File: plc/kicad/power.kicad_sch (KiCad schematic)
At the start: 29 parts, among them CN14 DB128V-5.08-2P-GN-S, U13 TPS54560DDAR, U15 TPS26630RGER

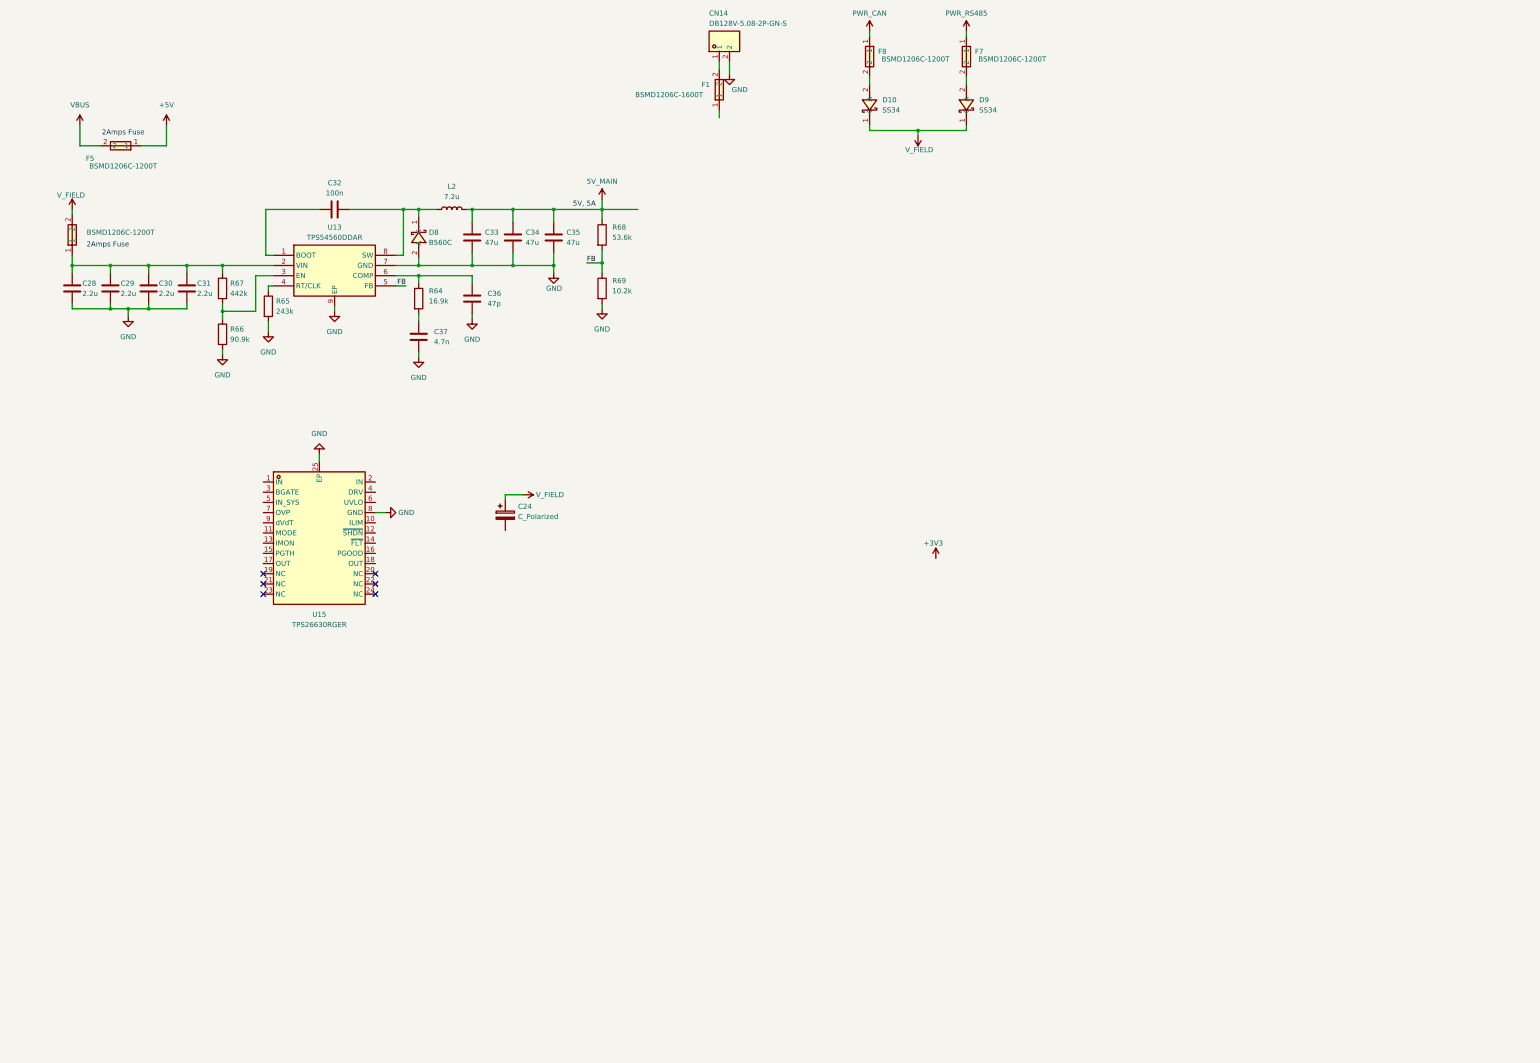
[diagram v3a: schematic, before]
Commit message: Added the power protection IC
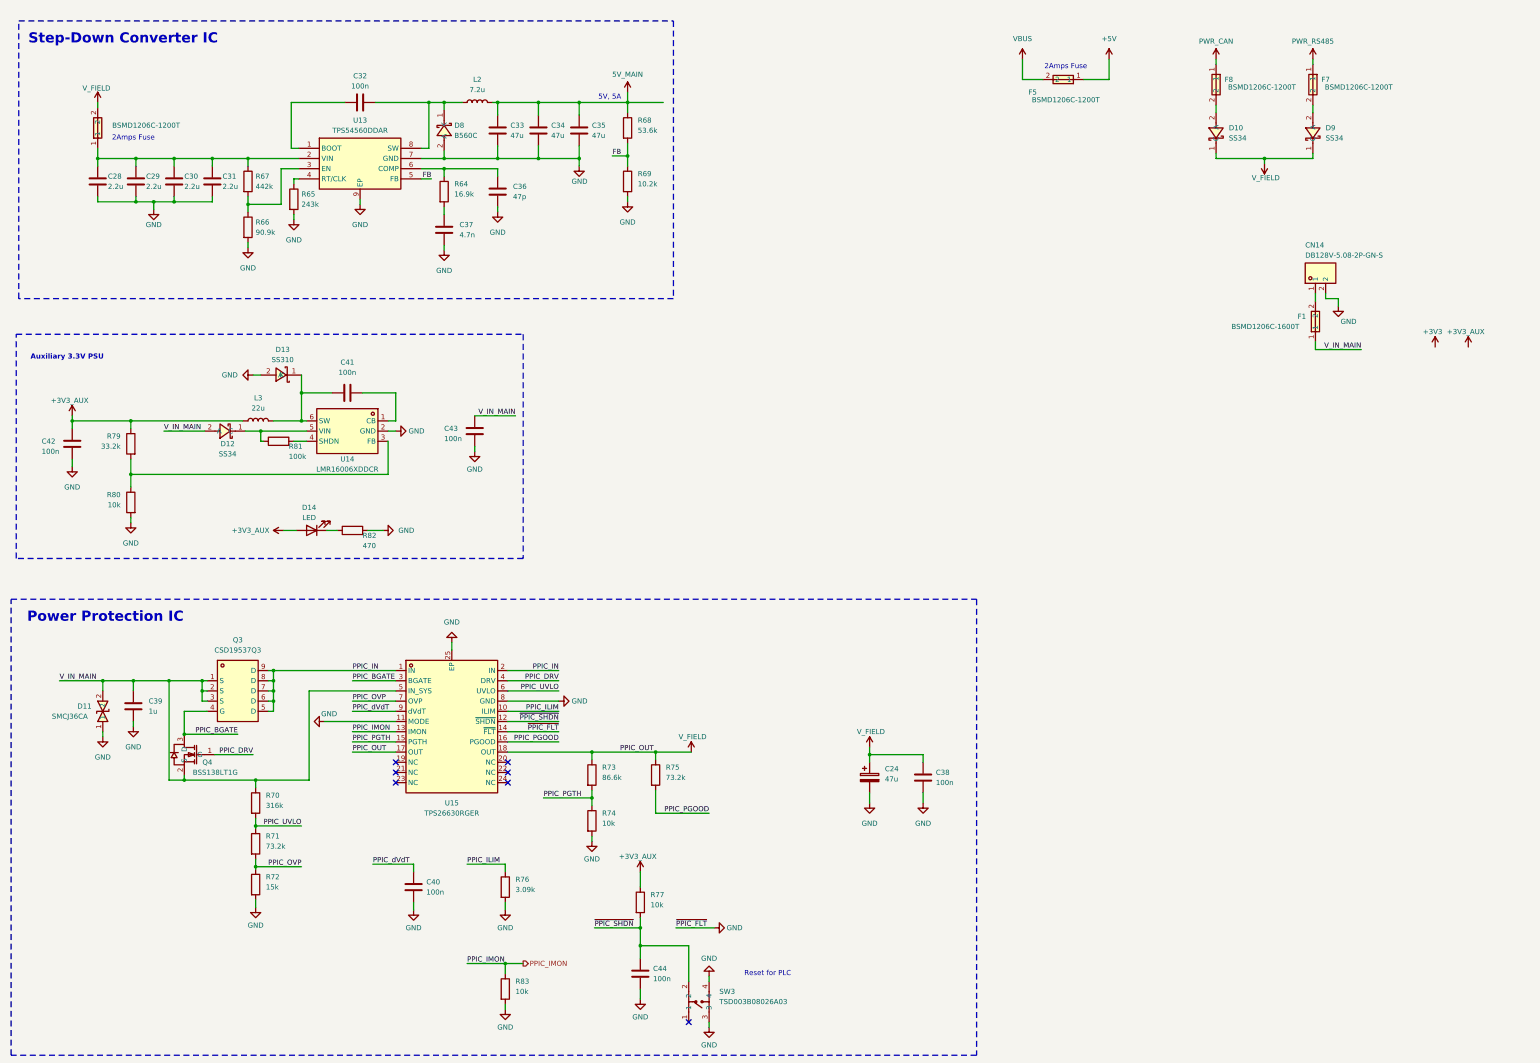
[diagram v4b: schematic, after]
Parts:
- added C38, C40, C41, C42, C43, C44: 100n, Capacitor_SMD:C_0805_2012Metric, symbol Device:C
- added C39: 1u, Capacitor_SMD:C_0805_2012Metric, symbol Device:C
- added D11: SMCJ36CA, LibrePLC32:SMC_L6.9-W5.9-LS7.9-BI, symbol LibrePLC32:SMCJ36CA-C151283
- added D12: SS34, LibrePLC32:SMA_L4.3-W2.7-LS5.1-RD, symbol LibrePLC32:SS34_C908680
- added D13: SS310, LibrePLC32:SMB_L4.6-W3.6-LS5.3-RD, symbol LibrePLC32:SS310_C14281
- added D14: LED, LED_SMD:LED_0805_2012Metric, symbol Device:LED
- added L3: 22u, symbol Device:L
- added Q3: CSD19537Q3, LibrePLC32:DFN-8_L3.3-W3.3-P0.65-BL-3, symbol LibrePLC32:CSD19537Q3
- added Q4: BSS138LT1G, LibrePLC32:SOT-23-3_L2.9-W1.6-P1.90-LS2.8-BR, symbol LibrePLC32:BSS138LT1G
- added R70: 316k, Resistor_SMD:R_0805_2012Metric, symbol Device:R
- added R71, R75: 73.2k, Resistor_SMD:R_0805_2012Metric, symbol Device:R
- added R72: 15k, Resistor_SMD:R_0805_2012Metric, symbol Device:R
- added R73: 86.6k, Resistor_SMD:R_0805_2012Metric, symbol Device:R
- added R74, R77, R80, R83: 10k, Resistor_SMD:R_0805_2012Metric, symbol Device:R
- added R76: 3.09k, Resistor_SMD:R_0805_2012Metric, symbol Device:R
- added R79: 33.2k, Resistor_SMD:R_0805_2012Metric, symbol Device:R
- added R81: 100k, Resistor_SMD:R_0805_2012Metric, symbol Device:R
- added R82: 470, Resistor_SMD:R_0805_2012Metric, symbol Device:R
- added SW3: TSD003B08026A03, LibrePLC32:SW-SMD_4P-L6.0-W6.0-P4.50-LS8.6, symbol LibrePLC32:TSD003B08026A03
- added U14: LMR16006XDDCR, LibrePLC32:SOT-23-6_L2.9-W1.6-P0.95-LS2.8-BR, symbol LibrePLC32:LMR16006XDDCR
- C24: value C_Polarized -> 47u
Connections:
- net GND: now also C24.2, U15.11 (MODE), U15.14 (~{FLT}), C38.1, C39.1, C40.1, C42.1, C43.1, C44.1, D11.1, D13.2 (A), R72.2, R74.2, R76.2, R80.2, R82.2, R83.2, SW3.3, SW3.4, U14.2 (GND)
- net V_FIELD: now also U15.17 (OUT), U15.18 (OUT), C38.2, R73.1, R75.1
- net V_IN_MAIN: now reaches F1.1
- net V_IN_MAIN: now also U15.5 (IN_SYS), C39.2, C43.2, D11.2, D12.2 (A), Q3.1 (S), Q3.2 (S), Q3.3 (S), Q4.2 (S), R70.1
- net PPIC_IN: now reaches U15.1 (IN)
- net PPIC_IN: now also U15.2 (IN), Q3.5 (D), Q3.6 (D), Q3.7 (D), Q3.8 (D), Q3.9 (D)
- net PPIC_ILIM: now reaches U15.10 (ILIM)
- net PPIC_ILIM: now also R76.1
- net ~{PPIC_SHDN}: now reaches U15.12 (~{SHDN})
- net ~{PPIC_SHDN}: now also C44.2, R77.2, SW3.2
- net PPIC_IMON: now reaches U15.13 (IMON)
- net PPIC_IMON: now also R83.1
- net PPIC_PGTH: now reaches U15.15 (PGTH)
- net PPIC_PGTH: now also R73.2, R74.1
- net PPIC_PGOOD: now reaches U15.16 (PGOOD)
- net PPIC_PGOOD: now also R75.2
- net PPIC_BGATE: now reaches U15.3 (BGATE)
- net PPIC_BGATE: now also Q3.4 (G), Q4.3 (D)
- net PPIC_DRV: now reaches U15.4 (DRV)
- net PPIC_DRV: now also Q4.1 (G)
- net PPIC_UVLO: now reaches U15.6 (UVLO)
- net PPIC_UVLO: now also R70.2, R71.1
- net PPIC_OVP: now reaches U15.7 (OVP)
- net PPIC_OVP: now also R71.2, R72.1
- net PPIC_dVdT: now reaches U15.9 (dVdT)
- net PPIC_dVdT: now also C40.2
- new net: R79.2, R80.1, U14.3 (FB)
- new net: D14.1 (K), R82.1
- new net: C41.1, U14.1 (CB)
- new net: C41.2, D13.1 (K), L3.1, U14.6 (SW)
- new net: R81.2, U14.4 (SHDN)
- new net: D12.1 (C), R81.1, U14.5 (VIN)
- new net +3V3_AUX: C42.2, D14.2 (A), L3.2, R77.1, R79.1
- no-connect marks 6 -> 7
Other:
- note added: "Auxiliary 3.3V PSU"
- note added: "Power Protection IC"
- note added: "Reset for PLC"
- note added: "Step-Down Converter IC"
- moved on the sheet: C24, C28, C29, C30, C31, C32, C33, C34, C35, C36, C37, CN14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

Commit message: Wired ESP32-S3 preliminarily
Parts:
- removed CN14: DB128V-5.08-2P-GN-S, LibrePLC32:CONN-TH_2P-P5.08_DIBO_DB128V-5.08, symbol LibrePLC32:DB128V-5.08-2P-GN-S
- removed F1: BSMD1206C-1600T, LibrePLC32:F1206, symbol LibrePLC32:BSMD1206C-1600T
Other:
- moved on the sheet: C24, C38, C40, R76, R83

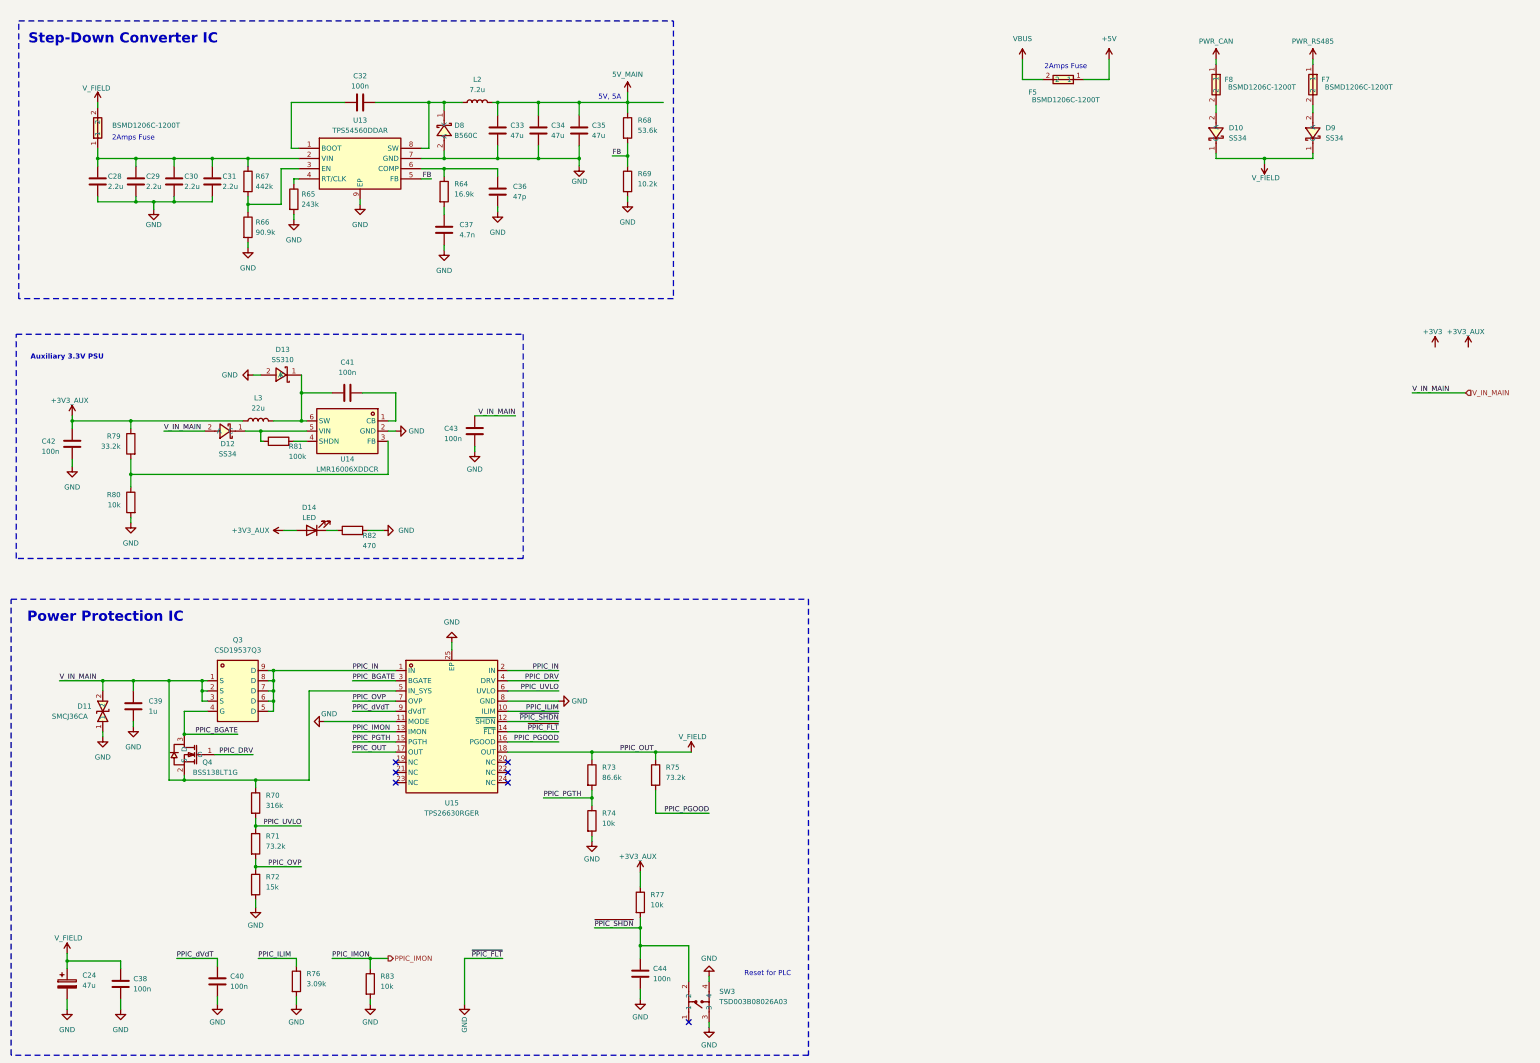
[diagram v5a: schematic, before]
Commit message: Added CP2102N bridge
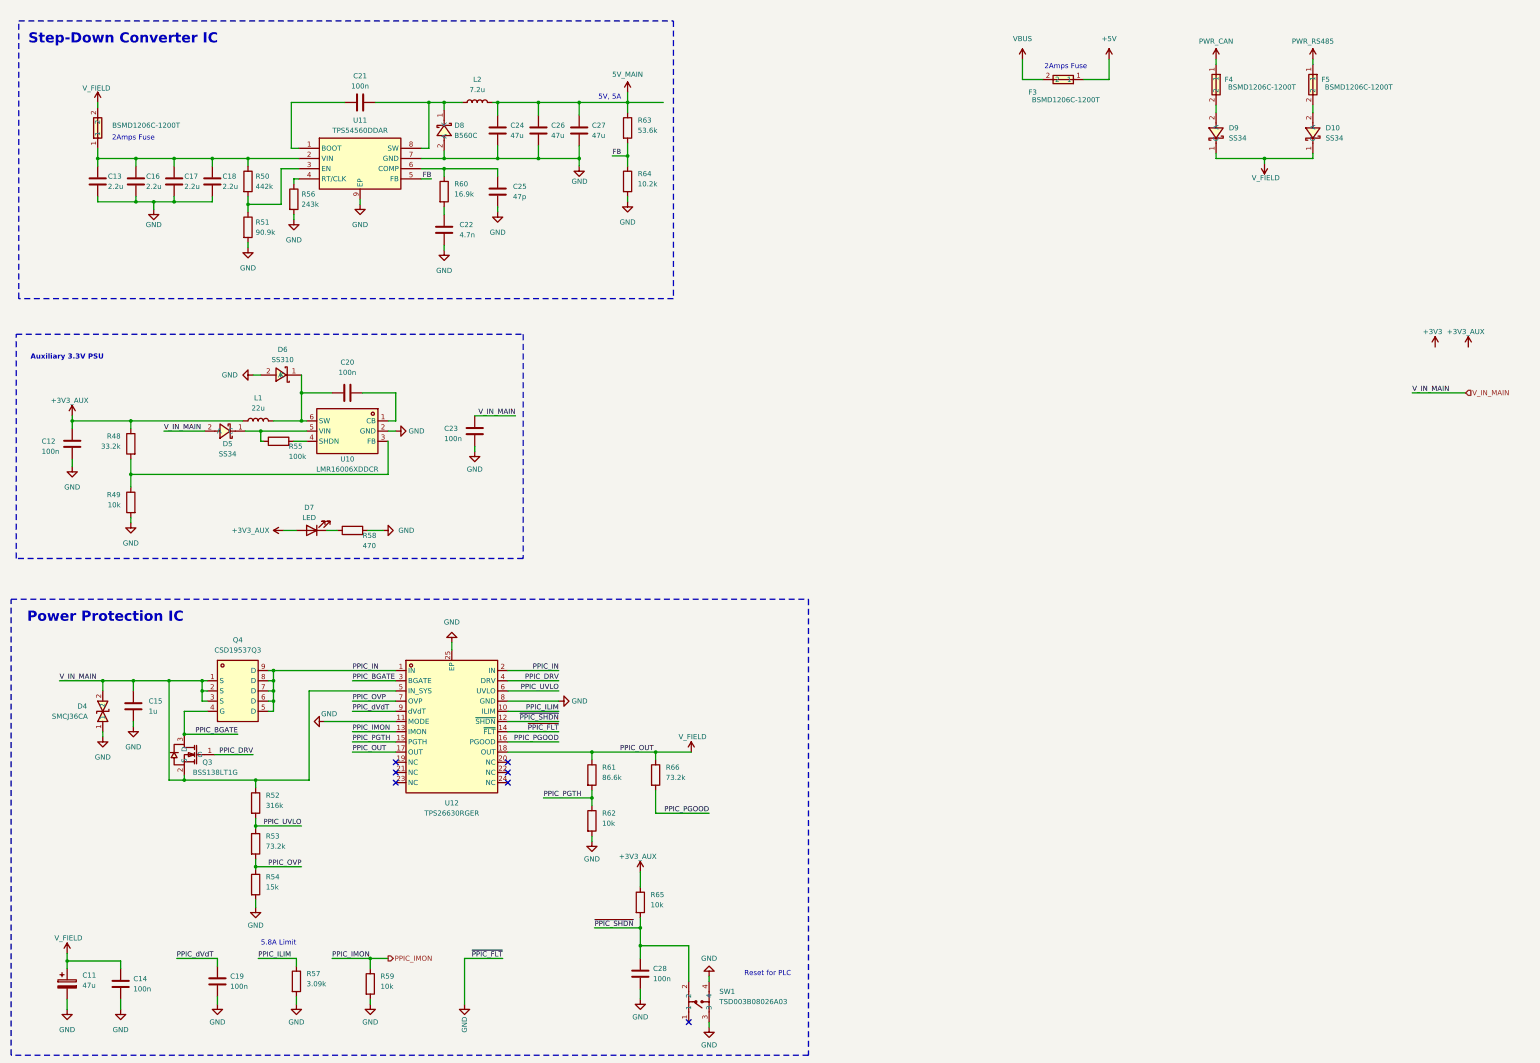
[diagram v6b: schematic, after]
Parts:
- renumbered C24 to C11, C42 to C12, C28 to C13, C38 to C14, C39 to C15, C29 to C16, C30 to C17, C31 to C18, C40 to C19, C41 to C20, C32 to C21, C37 to C22, C43 to C23, C33 to C24, C36 to C25, C34 to C26, C35 to C27, C44 to C28, D9 to D10, D11 to D4, D12 to D5, D13 to D6, D14 to D7, D10 to D9, F6 to F2, F5 to F3, F8 to F4, F7 to F5, L3 to L1, Q4 to Q3, Q3 to Q4, R79 to R48, R80 to R49, R67 to R50, R66 to R51, R70 to R52, R71 to R53, R72 to R54, R81 to R55, R65 to R56, R76 to R57, R82 to R58, R83 to R59, R64 to R60, R73 to R61, R74 to R62, R68 to R63, R69 to R64, R77 to R65, R75 to R66, SW3 to SW1, U14 to U10, U13 to U11, U15 to U12
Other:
- note added: "5.8A Limit"

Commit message: Added 3.3V regulator
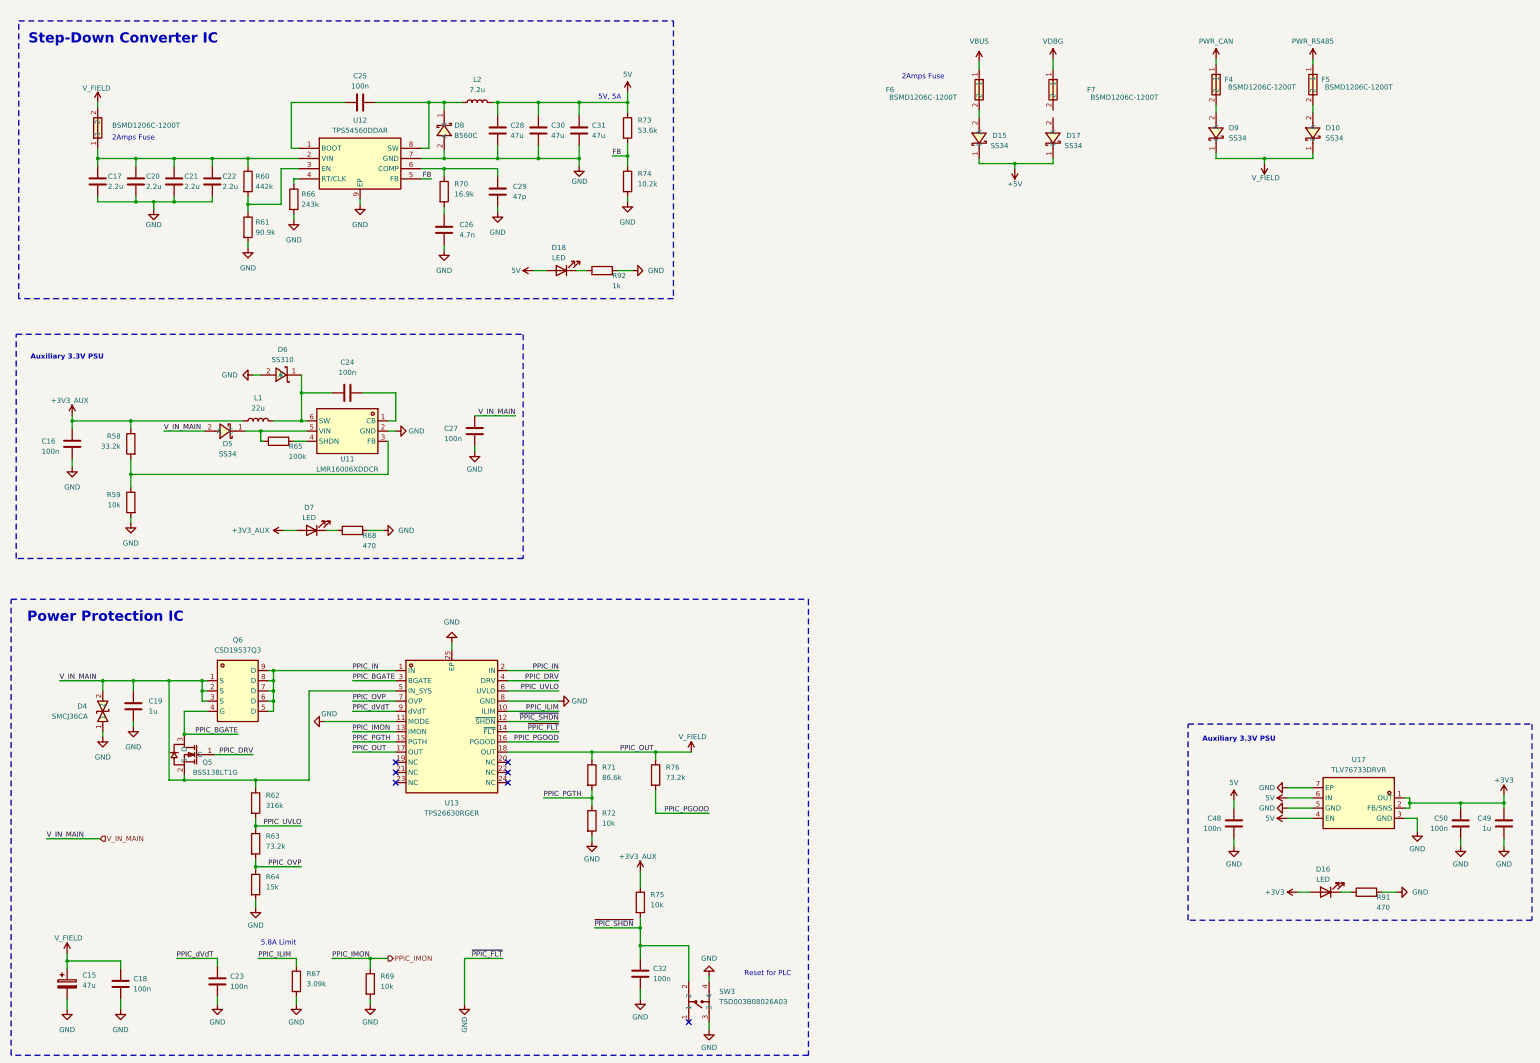
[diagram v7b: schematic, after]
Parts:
- removed F3: BSMD1206C-1200T, LibrePLC32:F1206, symbol LibrePLC32:BSMD1206C-1200T
- added C48, C50: 100n, Capacitor_SMD:C_0805_2012Metric, symbol Device:C
- added C49: 1u, Capacitor_SMD:C_0805_2012Metric, symbol Device:C
- added D15, D17: SS34, LibrePLC32:SMA_L4.3-W2.7-LS5.1-RD, symbol LibrePLC32:SS34_C908680
- added D16, D18: LED, LED_SMD:LED_0805_2012Metric, symbol Device:LED
- added F6, F7: BSMD1206C-1200T, LibrePLC32:F1206, symbol LibrePLC32:BSMD1206C-1200T
- added R91: 470, Resistor_SMD:R_0805_2012Metric, symbol Device:R
- added R92: 1k, Resistor_SMD:R_0805_2012Metric, symbol Device:R
- added U17: TLV76733DRVR, LibrePLC32:WSON-6_L2.0-W2.0-P0.65-TL-EP, symbol LibrePLC32:TLV76733DRVR
- renumbered C11 to C15, C12 to C16, C13 to C17, C14 to C18, C15 to C19, C16 to C20, C17 to C21, C18 to C22, C19 to C23, C20 to C24, C21 to C25, C22 to C26, C23 to C27, C24 to C28, C25 to C29, C26 to C30, C27 to C31, C28 to C32, Q3 to Q5, Q4 to Q6, R48 to R58, R49 to R59, R50 to R60, R51 to R61, R52 to R62, R53 to R63, R54 to R64, R55 to R65, R56 to R66, R57 to R67, R58 to R68, R59 to R69, R60 to R70, R61 to R71, R62 to R72, R63 to R73, R64 to R74, R65 to R75, R66 to R76, SW1 to SW3, U10 to U11, U11 to U12, U12 to U13
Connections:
- net +3V3: now also C49.2, C50.2, D16.2 (A), U17.1 (OUT), U17.2 (FB/SNS)
- net +5V: now also D15.1 (C), D17.1 (C)
- net GND: now also C48.1, C49.1, C50.1, R91.2, R92.2, U17.3 (GND), U17.5 (GND), U17.7 (EP)
- net VBUS: now also F6.1
- net 5V_MAIN renamed 5V
- net 5V: now also C48.2, D18.2 (A), U17.4 (EN), U17.6 (IN)
- new net: D15.2 (A), F6.2
- new net: D18.1 (K), R92.1
- new net: D16.1 (K), R91.1
- new net VDBG: F7.1
